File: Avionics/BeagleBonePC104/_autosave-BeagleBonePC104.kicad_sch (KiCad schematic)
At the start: 14 parts, among them U4 TJA1051T-3, U5 TMP36xS

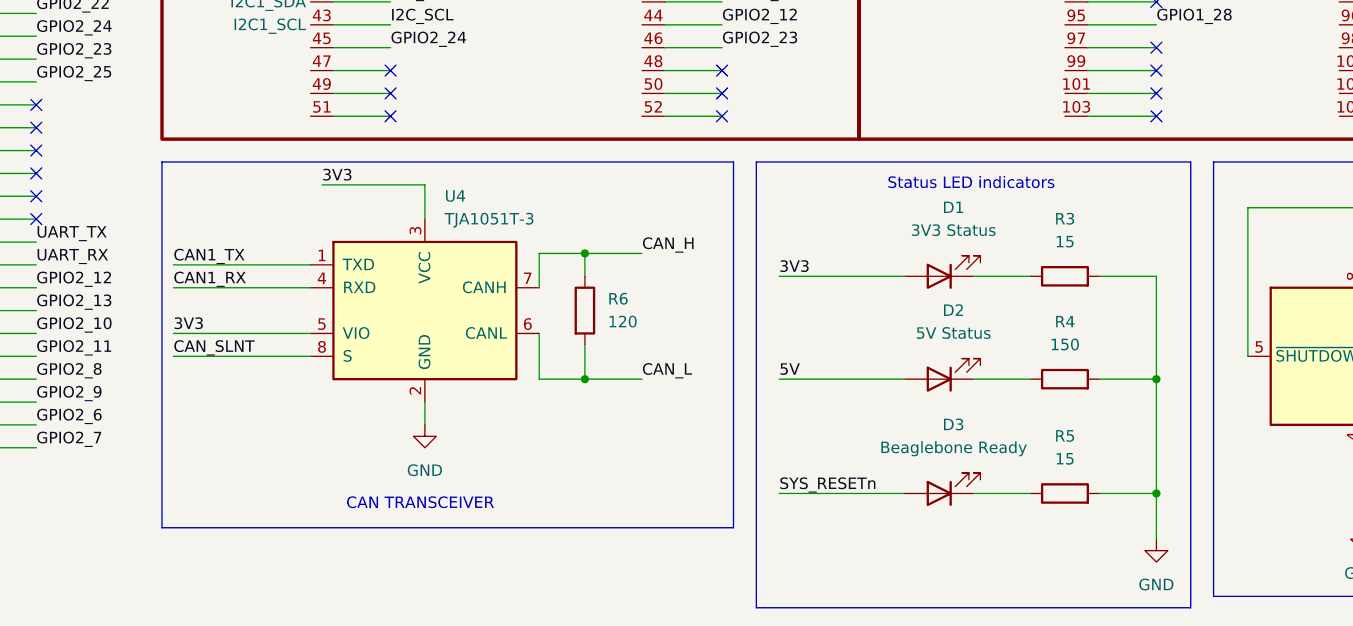
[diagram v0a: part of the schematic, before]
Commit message: Ian Goldberg - Made changes to the third revision of the flight computer board, trying to figure out a way to power it throught ht header connector while still extracting data (through ethernet).
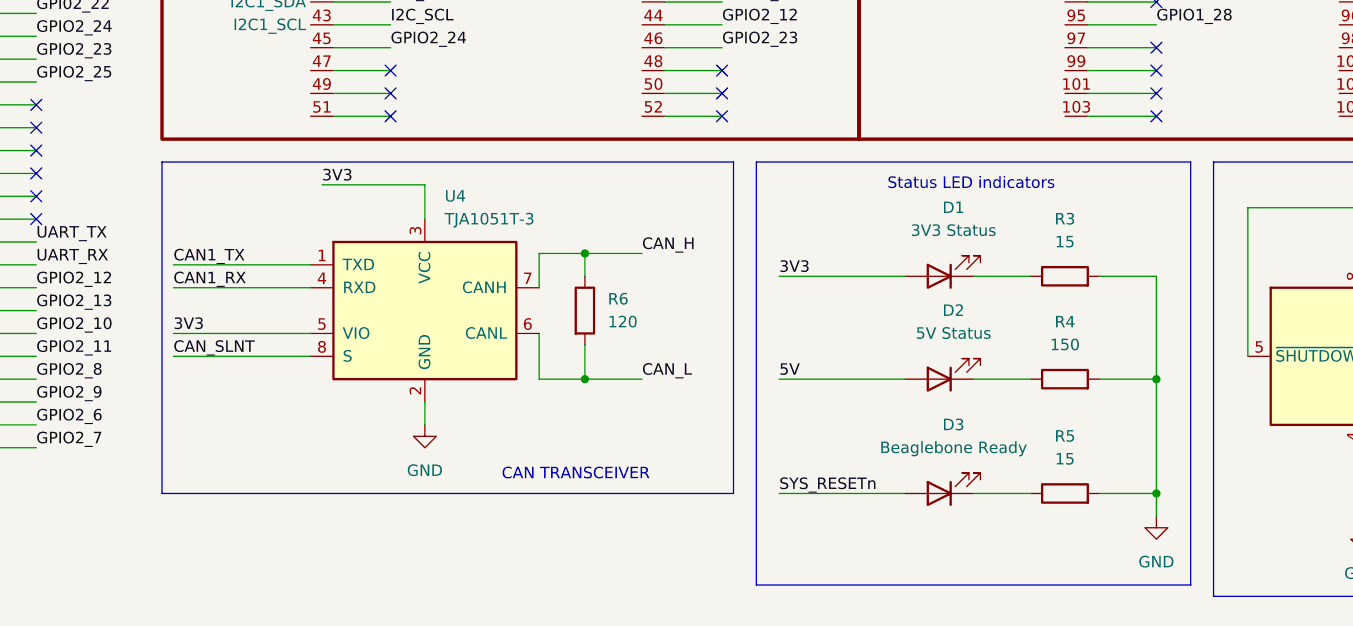
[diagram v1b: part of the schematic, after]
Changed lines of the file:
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@@
 	(wire
 		(pts
-			(xy 285.75 194.31) (xy 285.75 199.39)
+			(xy 285.75 194.31) (xy 285.75 196.85)
 		)
 		(stroke
@@
 	(rectangle
 		(start 175.26 157.48)
-		(end 238.76 198.12)
+		(end 238.76 194.31)
 		(stroke
 			(width 0)
@@
 	(rectangle
 		(start 241.3 157.48)
-		(end 289.56 207.01)
+		(end 289.56 204.47)
 		(stroke
 			(width 0)
@@
 	(text "CAN TRANSCEIVER"
 		(exclude_from_sim no)
-		(at 203.962 195.58 0)
+		(at 221.234 192.278 0)
 		(effects
 			(font
@@
 	(symbol
 		(lib_id "power:GND")
-		(at 285.75 199.39 0)
+		(at 285.75 196.85 0)
 		(unit 1)
 		(exclude_from_sim no)
@@
 		(fields_autoplaced yes)
 		(property "Reference" "#PWR06"
-			(at 285.75 205.74 0)
+			(at 285.75 203.2 0)
 			(effects
 				(font
@@
 		)
 		(property "Value" "GND"
-			(at 285.75 204.47 0)
+			(at 285.75 201.93 0)
 			(effects
 				(font
@@
 		)
 		(property "Footprint" ""
-			(at 285.75 199.39 0)
+			(at 285.75 196.85 0)
 			(effects
 				(font
@@
 		)
 		(property "Datasheet" ""
-			(at 285.75 199.39 0)
+			(at 285.75 196.85 0)
 			(effects
 				(font
@@
 		)
 		(property "Description" "Power symbol creates a global label with name \"GND\" , ground"
-			(at 285.75 199.39 0)
+			(at 285.75 196.85 0)
 			(effects
 				(font
